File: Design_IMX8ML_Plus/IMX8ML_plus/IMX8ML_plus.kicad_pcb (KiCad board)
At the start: 6 copper layers, 50 x 80 mm, 158 parts, among them J1 DF40C-100DP-0.4V_51_, J2 DF40C-100DP-0.4V_51_, J3 DF40C-100DP-0.4V_51_, J4 DF40C-100DP-0.4V_51_, U1 MIMX8ML8CVNKZAB, U2 MT53E1536M32D4DT-046 WT:A, U3 SDINBDG4-8G, U4 PCA9450CHNY, U5 MT25QUxxxxxx1xW7, U6 KSZ9131RNXI, Y1 32.768KHz, Y2 24MHz, Y3 32.768KHz

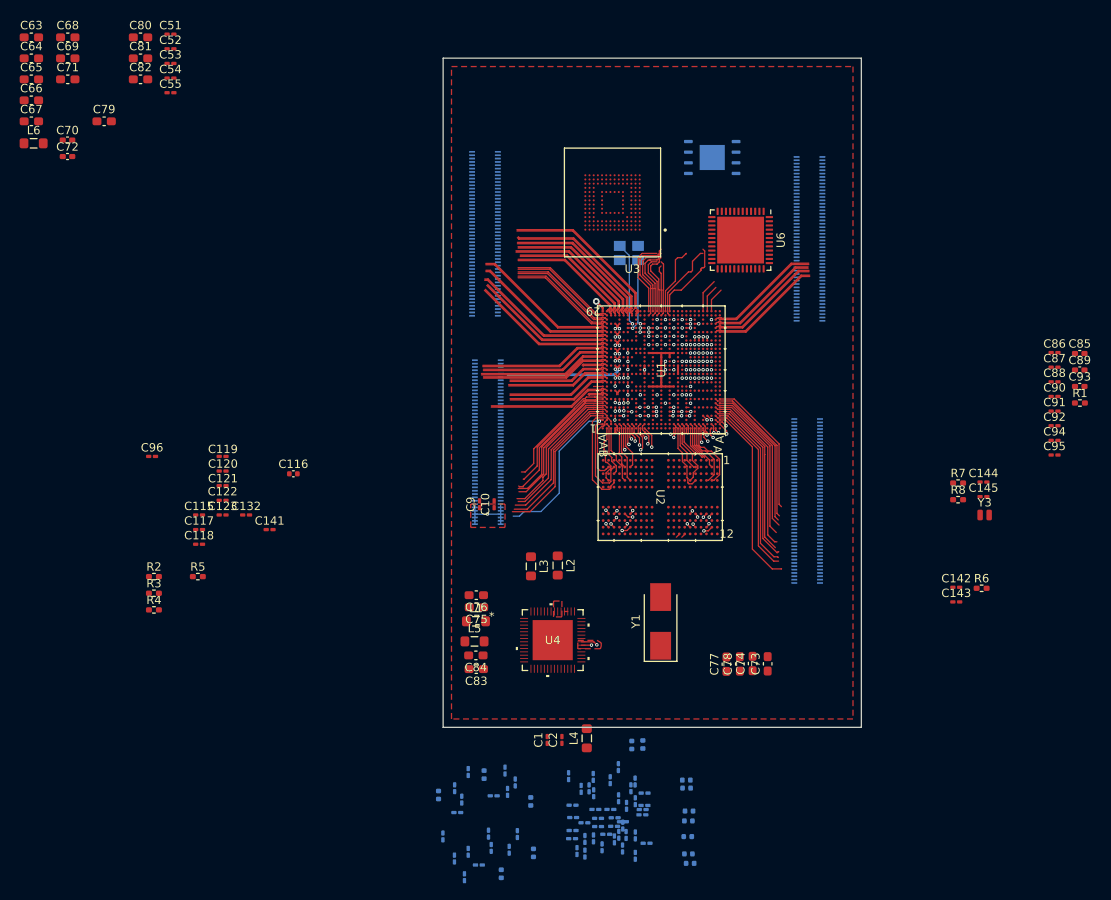
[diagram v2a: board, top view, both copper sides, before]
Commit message: Improve and fix connections in LPPDR4 memory
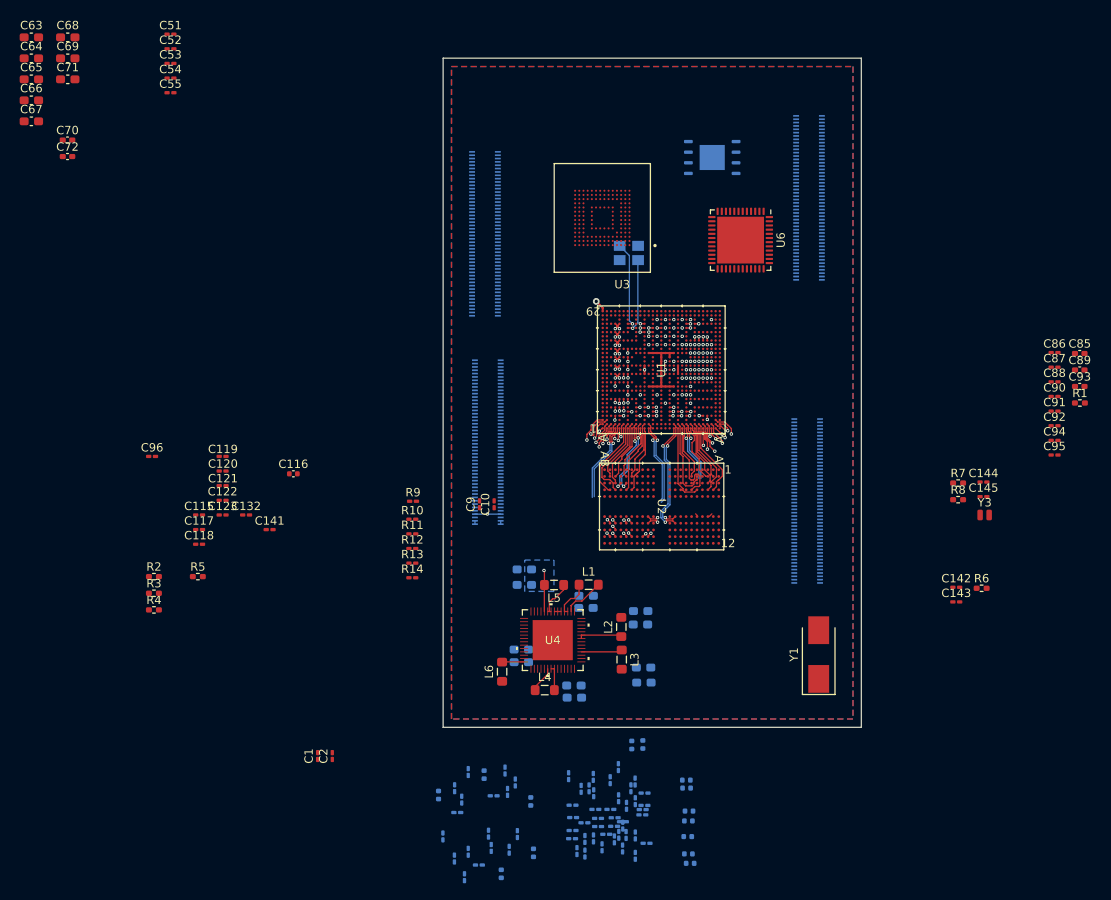
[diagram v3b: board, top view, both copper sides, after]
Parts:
- added R10: 240, Resistor_SMD:R_0201_0603Metric_Pad0.64x0.40mm_HandSolder, F.Cu at (106.3, 112.1)
- added R11: 10K, Resistor_SMD:R_0201_0603Metric_Pad0.64x0.40mm_HandSolder, F.Cu at (106.3, 113.9)
- added R12: 10K, Resistor_SMD:R_0201_0603Metric_Pad0.64x0.40mm_HandSolder, F.Cu at (106.3, 115.6)
- added R13: 10K, Resistor_SMD:R_0201_0603Metric_Pad0.64x0.40mm_HandSolder, F.Cu at (106.3, 117.4)
- added R14: 10K, Resistor_SMD:R_0201_0603Metric_Pad0.64x0.40mm_HandSolder, F.Cu at (106.3, 119.1)
- added R9: 240, Resistor_SMD:R_0201_0603Metric_Pad0.64x0.40mm_HandSolder, F.Cu at (106.4, 110.0)
- C73, C74, C75, C76, C77, C78, C79, C80, C81, C82, C83, C84: moved to B.Cu
- moved C80 94.5 mm to (125.7, 133.4)
- moved C79 87.8 mm to (125.6, 132.0)
- moved C81 85.3 mm to (119.3, 129.2)
- moved L6 84.4 mm to (117.0, 130.3), turned to 90 degrees
- moved C82 82.0 mm to (119.3, 127.7)
- moved C1 27.5 mm to (95.0, 140.4)
- moved C2 27.5 mm to (96.8, 140.4)
- moved Y1 19.3 mm to (154.9, 128.3)
- moved L3 15.6 mm to (131.3, 128.9)
- moved C73 14.8 mm to (134.0, 129.8), turned to 0 degrees
- moved L1 14.2 mm to (127.4, 120.0)
- moved C78 13.4 mm to (133.6, 123.1), turned to 0 degrees
- moved C83 13.2 mm to (119.7, 118.1)
- moved C74 13.2 mm to (134.0, 131.7), turned to 0 degrees
- moved C76 13.1 mm to (127.1, 121.3)
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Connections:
- U2 pad A4: NVCC_DRAM_1V1 -> PM_VDD_1V8
- U2 pad A5: unconnected-(U2A-ZQ0-PadA5) -> Net-(U2A-ZQ0)
- U2 pad A8: unconnected-(U2A-ZQ1-PadA8) -> Net-(U2A-ZQ1)
- U2 pad A9: NVCC_DRAM_1V1 -> PM_VDD_1V8
- U2 pad AA10: PM_VDD_1V8 -> NVCC_DRAM_1V1
- U2 pad AA11: /Processor/Up_memorie_lpddr4/DRAM_DATA8_A -> /Processor/Up_memorie_lpddr4/DRAM_DATA0_A
- U2 pad AA2: /Processor/Up_memorie_lpddr4/DRAM_DATA0_A -> /Processor/Up_memorie_lpddr4/DRAM_DATA8_A
- U2 pad AA3: PM_VDD_1V8 -> NVCC_DRAM_1V1
- U2 pad AA4: /Processor/Up_memorie_lpddr4/DRAM_DATA7_A -> /Processor/Up_memorie_lpddr4/DRAM_DATA15_A
- U2 pad AA5: PM_VDD_1V8 -> NVCC_DRAM_1V1
- U2 pad AA8: PM_VDD_1V8 -> NVCC_DRAM_1V1
- U2 pad AA9: /Processor/Up_memorie_lpddr4/DRAM_DATA15_A -> /Processor/Up_memorie_lpddr4/DRAM_DATA7_A
- U2 pad AB4: NVCC_DRAM_1V1 -> PM_VDD_1V8
- U2 pad AB9: NVCC_DRAM_1V1 -> PM_VDD_1V8
- U2 pad B10: PM_VDD_1V8 -> NVCC_DRAM_1V1
- U2 pad B3: PM_VDD_1V8 -> NVCC_DRAM_1V1
- U2 pad B5: PM_VDD_1V8 -> NVCC_DRAM_1V1
- U2 pad B8: PM_VDD_1V8 -> NVCC_DRAM_1V1
- U2 pad D1: PM_VDD_1V8 -> NVCC_DRAM_1V1
- U2 pad D12: PM_VDD_1V8 -> NVCC_DRAM_1V1
- U2 pad D5: PM_VDD_1V8 -> NVCC_DRAM_1V1
- U2 pad D8: PM_VDD_1V8 -> NVCC_DRAM_1V1
- U2 pad F10: PM_VDD_1V8 -> NVCC_DRAM_1V1
- U2 pad F3: PM_VDD_1V8 -> NVCC_DRAM_1V1
- U2 pad F5: NVCC_DRAM_1V1 -> PM_VDD_1V8
- U2 pad F8: NVCC_DRAM_1V1 -> PM_VDD_1V8
- U2 pad G2: unconnected-(U2A-ODT_CA_A-PadG2) -> NVCC_DRAM_1V1
- U2 pad H1: NVCC_DRAM_1V1 -> PM_VDD_1V8
- U2 pad H12: NVCC_DRAM_1V1 -> PM_VDD_1V8
- U2 pad H5: NVCC_DRAM_1V1 -> PM_VDD_1V8
- U2 pad H8: NVCC_DRAM_1V1 -> PM_VDD_1V8
- U2 pad K1: NVCC_DRAM_1V1 -> PM_VDD_1V8
- U2 pad K10: NVCC_DRAM_1V1 -> PM_VDD_1V8
- U2 pad K12: NVCC_DRAM_1V1 -> PM_VDD_1V8
- U2 pad K3: NVCC_DRAM_1V1 -> PM_VDD_1V8
- U2 pad N1: NVCC_DRAM_1V1 -> PM_VDD_1V8
- U2 pad N10: NVCC_DRAM_1V1 -> PM_VDD_1V8
- U2 pad N12: NVCC_DRAM_1V1 -> PM_VDD_1V8
- U2 pad N3: NVCC_DRAM_1V1 -> PM_VDD_1V8
- U2 pad R1: NVCC_DRAM_1V1 -> PM_VDD_1V8
- U2 pad R12: NVCC_DRAM_1V1 -> PM_VDD_1V8
- U2 pad R5: NVCC_DRAM_1V1 -> PM_VDD_1V8
- U2 pad R8: NVCC_DRAM_1V1 -> PM_VDD_1V8
- U2 pad T2: unconnected-(U2B-ODT_CA_B-PadT2) -> NVCC_DRAM_1V1
- U2 pad U10: PM_VDD_1V8 -> NVCC_DRAM_1V1
- U2 pad U11: /Processor/Up_memorie_lpddr4/DRAM_DATA11_A -> /Processor/Up_memorie_lpddr4/DRAM_DATA3_A
- U2 pad U2: /Processor/Up_memorie_lpddr4/DRAM_DATA3_A -> /Processor/Up_memorie_lpddr4/DRAM_DATA12_A
- U2 pad U3: PM_VDD_1V8 -> NVCC_DRAM_1V1
- U2 pad U4: /Processor/Up_memorie_lpddr4/DRAM_DATA4_A -> /Processor/Up_memorie_lpddr4/DRAM_DATA13_A
- U2 pad U5: NVCC_DRAM_1V1 -> PM_VDD_1V8
- U2 pad U8: NVCC_DRAM_1V1 -> PM_VDD_1V8
- U2 pad U9: /Processor/Up_memorie_lpddr4/DRAM_DATA12_A -> /Processor/Up_memorie_lpddr4/DRAM_DATA4_A
- U2 pad V10: /Processor/Up_memorie_lpddr4/DRAM_SDQS1_A- -> /Processor/Up_memorie_lpddr4/DRAM_SDQS0_A-
- U2 pad V11: /Processor/Up_memorie_lpddr4/DRAM_DATA10_A -> /Processor/Up_memorie_lpddr4/DRAM_DATA2_A
- U2 pad V2: /Processor/Up_memorie_lpddr4/DRAM_DATA2_A -> /Processor/Up_memorie_lpddr4/DRAM_DATA11_A
- U2 pad V3: /Processor/Up_memorie_lpddr4/DRAM_SDQS0_A- -> /Processor/Up_memorie_lpddr4/DRAM_SDQS1_A-
- U2 pad V4: /Processor/Up_memorie_lpddr4/DRAM_DATA5_A -> /Processor/Up_memorie_lpddr4/DRAM_DATA10_A
- U2 pad V9: /Processor/Up_memorie_lpddr4/DRAM_DATA13_A -> /Processor/Up_memorie_lpddr4/DRAM_DATA5_A
- U2 pad W1: PM_VDD_1V8 -> NVCC_DRAM_1V1
- U2 pad W10: /Processor/Up_memorie_lpddr4/DRAM_SDQS1_A+ -> /Processor/Up_memorie_lpddr4/DRAM_SDQS0_A+
- U2 pad W12: PM_VDD_1V8 -> NVCC_DRAM_1V1
- U2 pad W3: /Processor/Up_memorie_lpddr4/DRAM_SDQS0_A+ -> /Processor/Up_memorie_lpddr4/DRAM_SDQS1_A+
- U2 pad W5: PM_VDD_1V8 -> NVCC_DRAM_1V1
- U2 pad W8: PM_VDD_1V8 -> NVCC_DRAM_1V1
- U2 pad Y10: /Processor/Up_memorie_lpddr4/DRAM_DMI1_A -> /Processor/Up_memorie_lpddr4/DRAM_DMI0_A
- U2 pad Y11: /Processor/Up_memorie_lpddr4/DRAM_DATA9_A -> /Processor/Up_memorie_lpddr4/DRAM_DATA1_A
- U2 pad Y2: /Processor/Up_memorie_lpddr4/DRAM_DATA1_A -> /Processor/Up_memorie_lpddr4/DRAM_DATA9_A
- U2 pad Y3: /Processor/Up_memorie_lpddr4/DRAM_DMI0_A -> /Processor/Up_memorie_lpddr4/DRAM_DMI1_A
- U2 pad Y4: /Processor/Up_memorie_lpddr4/DRAM_DATA6_A -> /Processor/Up_memorie_lpddr4/DRAM_DATA14_A
- U2 pad Y9: /Processor/Up_memorie_lpddr4/DRAM_DATA14_A -> /Processor/Up_memorie_lpddr4/DRAM_DATA6_A
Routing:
- net /Processor/storage/QSPIA_DATA3: track 33.5 -> 0.49 mm
- net /Processor/storage/QSPIA_SCLK: track 30.4 -> 0.50 mm
- net /Processor/storage/QSPIA_DATA0: track 29.7 -> 0.49 mm
- net /Processor/storage/QSPIA_nSS0: track 26.0 -> 0.50 mm
- net /Processor/storage/QSPIA_DATA1: track 25.3 -> 0.50 mm
- net /Processor/storage/QSPIA_DATA2: track 24.4 -> 0.53 mm
- net CSI1_D0_N: track 23.7 -> 0.57 mm
- net CSI1_D0_P: track 23.3 -> 0.57 mm
- net CSI1_D1_N: track 22.7 -> 0.73 mm
- net UART1_TXD: track 21.9 -> 0.00 mm
- net CSI1_D1_P: track 22.3 -> 0.73 mm
- net UART2_TXD: track 21.5 -> 0.00 mm
- net UART4_TXD: track 21.0 -> 0.00 mm
- net GPIO1_IO07: track 21.2 -> 0.41 mm
- net UART3_TXD: track 20.7 -> 0.00 mm
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- added copper zone on B.Cu, net GND
- added copper zone on In3.Cu, net GND
- added copper zone on B.Cu, net NVCC_DRAM_1V1
- removed copper zone on F.Cu, net VDD_SYS
- removed copper zone on In2.Cu, net VDD_SYS

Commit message: Add Base board IMxM8ML project
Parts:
- added R15: 240, Resistor_SMD:R_0201_0603Metric_Pad0.64x0.40mm_HandSolder, F.Cu at (106.1, 105.6)
- added R16: 10K, Resistor_SMD:R_0201_0603Metric_Pad0.64x0.40mm_HandSolder, F.Cu at (106.1, 107.3)
- U6: moved to B.Cu
- moved U5 14.0 mm to (129.1, 63.9)
- moved U3 3.17 mm to (127.4, 73.4)
- moved Y2 3.03 mm to (132.4, 83.3)
- moved U6 1.81 mm to (144.2, 79.9)
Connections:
- J4 pad 80: unconnected-(J4-Pad80) -> ECSPI1_MISO
- J4 pad 82: unconnected-(J4-Pad82) -> ECSPI1_MOSI
- J4 pad 84: unconnected-(J4-Pad84) -> ECSPI1_SCLK
- J4 pad 85: unconnected-(J4-Pad85) -> EARC_AUX
- J4 pad 86: unconnected-(J4-Pad86) -> ECSPI1_SSO
- J4 pad 87: unconnected-(J4-Pad87) -> EARC_N_HPD
- J4 pad 88: unconnected-(J4-Pad88) -> ECSPI2_MISO
- J4 pad 89: unconnected-(J4-Pad89) -> EARC_P_UTIL
- J4 pad 90: unconnected-(J4-Pad90) -> ECSPI2_MOSI
- J4 pad 92: unconnected-(J4-Pad92) -> ECSPI2_SCLK
- J4 pad 94: unconnected-(J4-Pad94) -> ECSPI2_SSO
- U1 pad AC20: unconnected-(U1B-ECSPI1_MOSI-PadAC20) -> ECSPI1_MOSI
- U1 pad AD20: unconnected-(U1B-ECSPI1_MISO-PadAD20) -> ECSPI1_MISO
- U1 pad AE20: unconnected-(U1B-ECSPI1_SS0-PadAE20) -> ECSPI1_SSO
- U1 pad AF20: unconnected-(U1B-ECSPI1_SCLK-PadAF20) -> ECSPI1_SCLK
- U1 pad AH20: unconnected-(U1B-ECSPI2_MISO-PadAH20) -> ECSPI2_MISO
- U1 pad AH21: unconnected-(U1B-ECSPI2_SCLK-PadAH21) -> ECSPI2_SCLK
- U1 pad AH22: unconnected-(U1B-EARC_N_HPD-PadAH22) -> EARC_N_HPD
- U1 pad AH23: unconnected-(U1B-EARC_AUX-PadAH23) -> EARC_AUX
- U1 pad AJ21: unconnected-(U1B-ECSPI2_MOSI-PadAJ21) -> ECSPI2_MOSI
- U1 pad AJ22: unconnected-(U1B-ECSPI2_SS0-PadAJ22) -> ECSPI2_SSO
- U1 pad AJ23: unconnected-(U1B-EARC_P_UTIL-PadAJ23) -> EARC_P_UTIL
- U1 pad R1: unconnected-(U1B-DRAM_ZN-PadR1) -> Net-(U1B-DRAM_ZN)
- U1 pad T1: unconnected-(U1B-DRAM_RESET_N-PadT1) -> Net-(U1B-DRAM_RESET_N)
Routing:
- net GPIO1_IO05: track 0.00 -> 19.6 mm
- net GPIO1_IO15: track 0.00 -> 18.5 mm
- net GPIO1_IO14: track 0.00 -> 18.3 mm
- net GPIO1_IO02: track 0.00 -> 18.1 mm
- net GPIO1_IO12: track 0.00 -> 17.8 mm
- net GPIO1_IO10: track 0.00 -> 17.5 mm
- net GPIO1_IO09: track 0.00 -> 17.4 mm
- net GPIO1_IO13: track 0.00 -> 17.3 mm
- net GPIO1_IO00: track 0.00 -> 17.1 mm
- net GPIO1_IO08: track 0.00 -> 16.7 mm
- net PCIE_RXN_N: track 0.00 -> 16.3 mm
- net PCIE_TXN_N: track 0.00 -> 16.3 mm
- net PCIE_RXN_P: track 0.00 -> 15.7 mm
- net PCIE_TXN_P: track 0.00 -> 15.7 mm
- net Net-(U1F-XTALO_24M): track 10.5 -> 0.55 mm
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
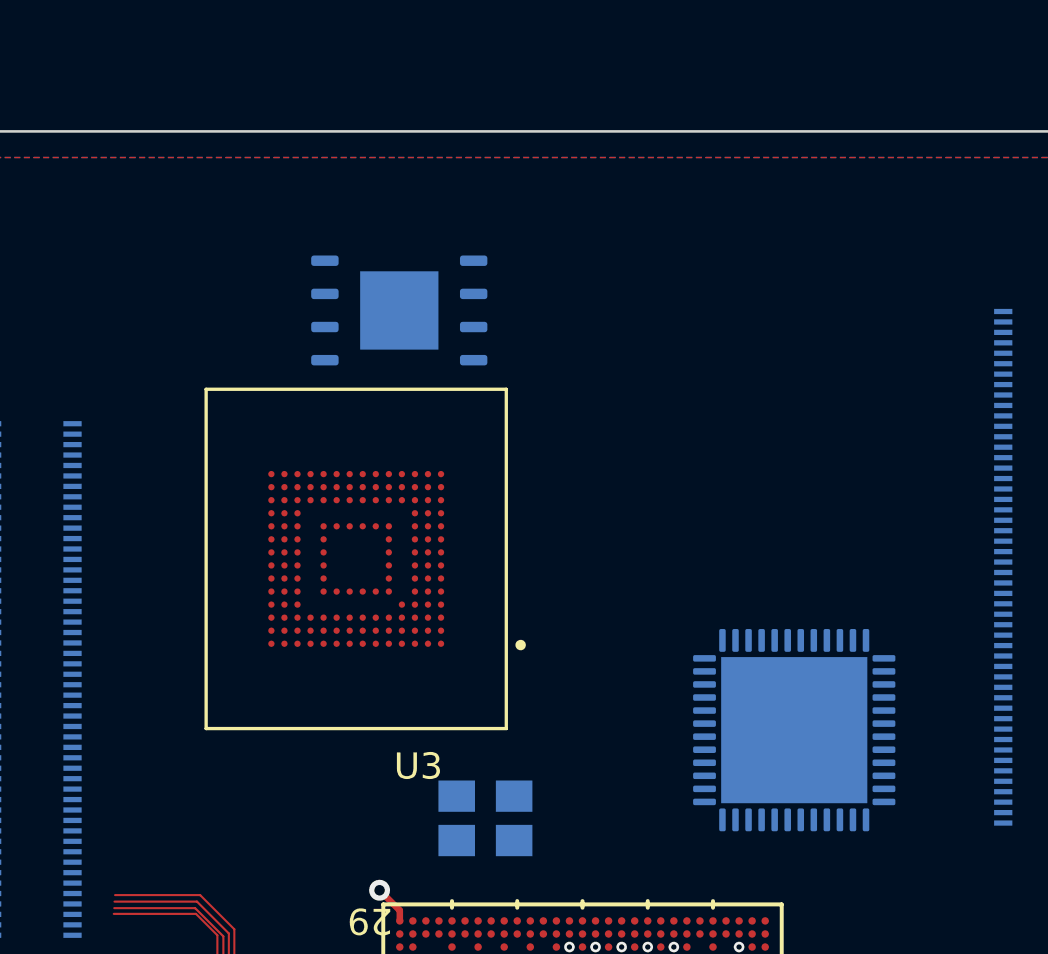
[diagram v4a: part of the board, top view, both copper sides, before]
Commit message: Add SPB228 WIFI/BLE module
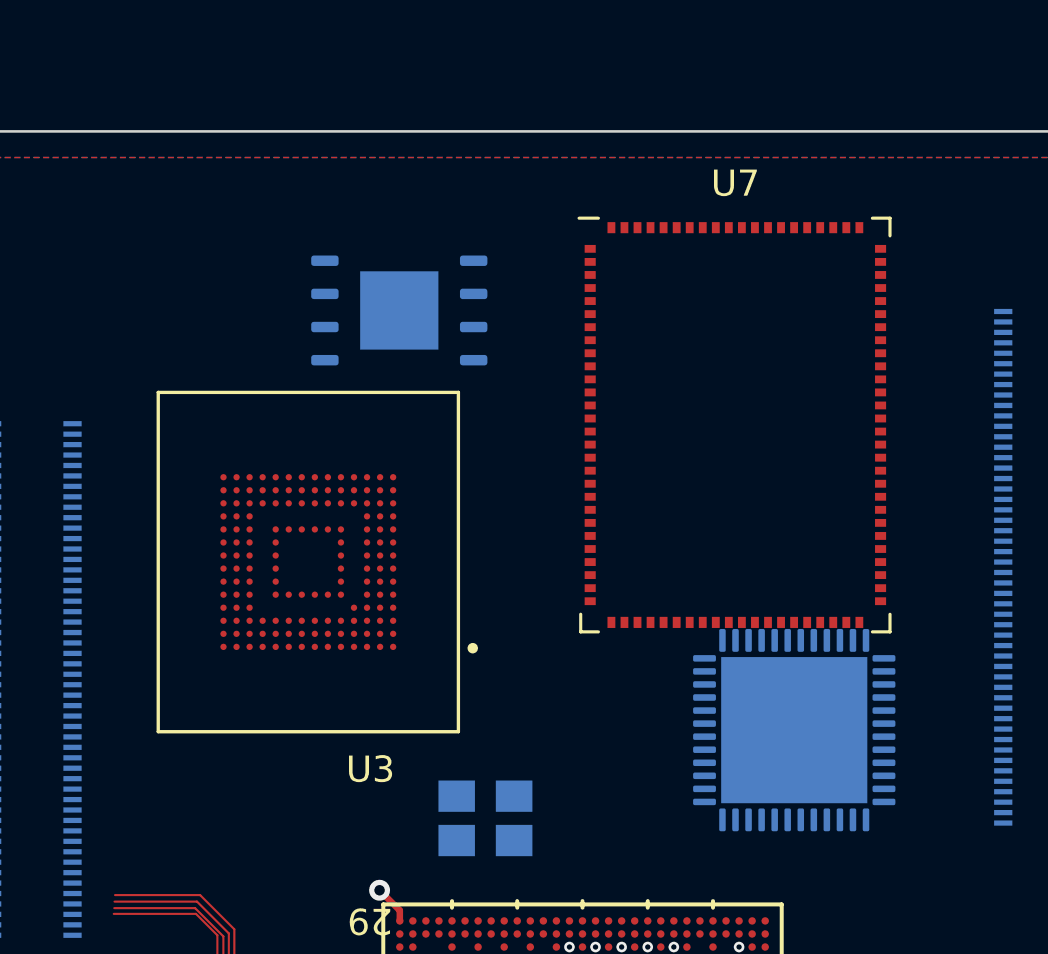
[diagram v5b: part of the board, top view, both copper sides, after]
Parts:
- added U7: ~, _W_SBC:SPB228-QFN-96_11.55x15.55_Pitch0.5mm, F.Cu at (141.9, 68.2)
- moved U3 1.84 mm to (125.6, 73.5)

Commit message: Improve power source module in the base board
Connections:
- J2 pad 70: SDC2_WP -> unconnected-(J2-Pad70)
- J2 pad 72: SDC2_RESET_B -> unconnected-(J2-Pad72)
- J2 pad 74: SDC2_DATA3 -> unconnected-(J2-Pad74)
- J2 pad 76: SDC2_DATA2 -> unconnected-(J2-Pad76)
- J2 pad 78: SDC2_DATA1 -> unconnected-(J2-Pad78)
- J2 pad 80: SDC2_DATA0 -> unconnected-(J2-Pad80)
- J2 pad 82: SDC2_CMD -> unconnected-(J2-Pad82)
- J2 pad 84: SDC2_CLK -> unconnected-(J2-Pad84)
- J2 pad 86: SDC2_CD_B -> unconnected-(J2-Pad86)
- U7 pad 1: Net-(U7-nc-Pad1) -> unconnected-(U7-nc-Pad1)_8
- U7 pad 14: Net-(U7-nc-Pad1) -> unconnected-(U7-nc-Pad1)_3
- U7 pad 16: Net-(U7-nc-Pad1) -> unconnected-(U7-nc-Pad1)_5
- U7 pad 17: GND -> Net-(U7-GND-Pad17)
- U7 pad 19: Net-(U7-nc-Pad1) -> unconnected-(U7-nc-Pad1)_2
- U7 pad 2: Net-(U7-nc-Pad1) -> unconnected-(U7-nc-Pad1)_7
- U7 pad 20: GND -> Net-(U7-GND-Pad17)
- U7 pad 23: GND -> Net-(U7-GND-Pad17)
- U7 pad 25: Net-(U7-nc-Pad1) -> unconnected-(U7-nc-Pad1)_6
- U7 pad 26: GND -> Net-(U7-GND-Pad17)
- U7 pad 3: Net-(U7-nc-Pad1) -> unconnected-(U7-nc-Pad1)_4
- U7 pad 32: GND -> Net-(U7-GND-Pad17)
- U7 pad 35: GND -> Net-(U7-GND-Pad32)
- U7 pad 38: GND -> Net-(U7-GND-Pad32)
- U7 pad 41: GND -> Net-(U7-GND-Pad32)
- U7 pad 43: Net-(U7-nc-Pad1) -> unconnected-(U7-nc-Pad1)
- U7 pad 47: unconnected-(U7-SD_DAT3-Pad47) -> SDC2_DATA3
- U7 pad 48: unconnected-(U7-SD_DAT2-Pad48) -> SDC2_DATA1
- U7 pad 49: unconnected-(U7-SD_DAT0-Pad49) -> SDC2_DATA0
- U7 pad 51: unconnected-(U7-SD_CMD-Pad51) -> SDC2_CMD
- U7 pad 52: unconnected-(U7-SD_CLK-Pad52) -> SDC2_CLK
- U7 pad 6: GND -> Net-(U7-GND-Pad17)
- U7 pad 62: GND -> Net-(U7-GND-Pad17)
- U7 pad 67: Net-(U7-nc-Pad1) -> unconnected-(U7-nc-Pad1)_9
- U7 pad 68: GND -> Net-(U7-GND-Pad17)
- U7 pad 7: Net-(U7-nc-Pad1) -> unconnected-(U7-nc-Pad1)_1
- U7 pad 71: GND -> Net-(U7-GND-Pad17)
- U7 pad 74: GND -> Net-(U7-GND-Pad17)
- U7 pad 75: GND -> Net-(U7-GND-Pad17)
- U7 pad 76: GND -> Net-(U7-GND-Pad17)
- U7 pad 77: GND -> Net-(U7-GND-Pad17)
- U7 pad 78: GND -> Net-(U7-GND-Pad17)
- U7 pad 79: GND -> Net-(U7-GND-Pad17)
- U7 pad 80: GND -> Net-(U7-GND-Pad17)
- U7 pad 81: GND -> Net-(U7-GND-Pad17)
- U7 pad 82: GND -> Net-(U7-GND-Pad17)
- U7 pad 83: GND -> Net-(U7-GND-Pad17)
- U7 pad 84: GND -> Net-(U7-GND-Pad17)
- U7 pad 85: GND -> Net-(U7-GND-Pad17)
- U7 pad 86: GND -> Net-(U7-GND-Pad17)
- U7 pad 87: GND -> Net-(U7-GND-Pad17)
- U7 pad 89: GND -> Net-(U7-GND-Pad17)
- U7 pad 90: GND -> Net-(U7-GND-Pad17)
- U7 pad 91: GND -> Net-(U7-GND-Pad17)
- U7 pad 92: GND -> Net-(U7-GND-Pad17)
- U7 pad 93: GND -> Net-(U7-GND-Pad17)
- U7 pad 94: GND -> Net-(U7-GND-Pad17)
- U7 pad 95: GND -> Net-(U7-GND-Pad17)
- U7 pad 96: GND -> Net-(U7-GND-Pad17)
